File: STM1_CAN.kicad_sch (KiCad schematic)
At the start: 18 parts, among them J6 Conn_01x04, U1 STM32F072C8Tx, U2 TJA1051T-3

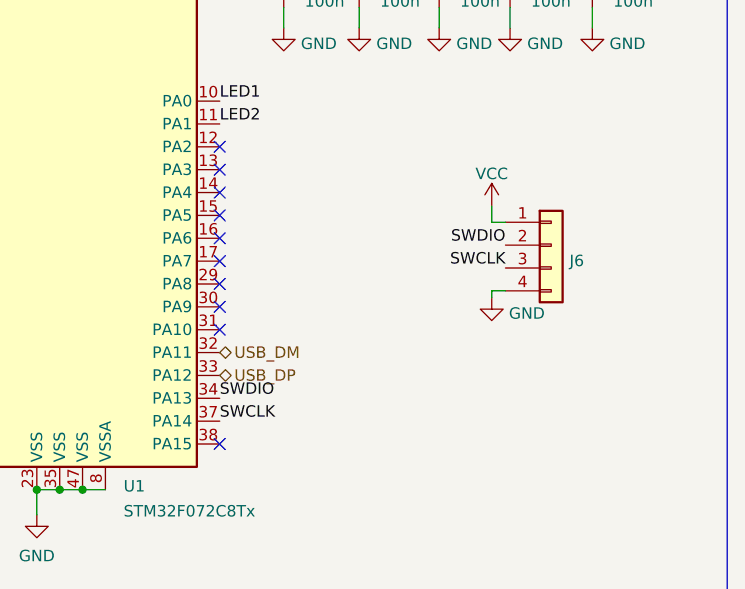
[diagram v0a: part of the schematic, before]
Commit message: New PCB design and single panel to SMT
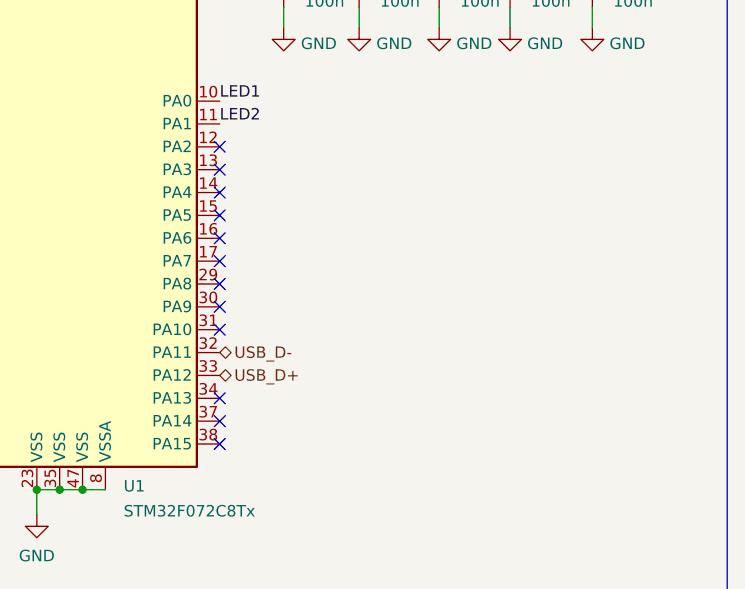
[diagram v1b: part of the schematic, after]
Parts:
- removed J6: Conn_01x04, Connector_JST:JST_GH_BM04B-GHS-TBT_1x04-1MP_P1.25mm_Vertical, symbol Connector_Generic:Conn_01x04
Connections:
- net SWCLK: no longer names the net of U1.37 (PA14)
- net SWDIO: no longer names the net of U1.34 (PA13)
- net USB_DM renamed USB_D-
- net USB_DP renamed USB_D+
- no-connect marks 29 -> 31
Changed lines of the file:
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@@
   (no_connect (at 87.884 84.074))
   (no_connect (at 54.864 99.314))
+  (no_connect (at 87.884 101.854))
+  (no_connect (at 87.884 104.394))
   (no_connect (at 87.884 91.694))
   (no_connect (at 87.884 86.614))
@@
     (stroke (width 0) (type default) (color 0 0 0 0))
   )
-  (wire (pts (xy 118.11 90.678) (xy 118.11 89.916))
-    (stroke (width 0) (type default) (color 0 0 0 0))
-  )
   (wire (pts (xy 112.268 50.8) (xy 112.268 53.34))
     (stroke (width 0) (type default) (color 0 0 0 0))
@@
     (stroke (width 0) (type default) (color 0 0 0 0))
   )
-  (wire (pts (xy 118.11 89.916) (xy 119.634 89.916))
-    (stroke (width 0) (type default) (color 0 0 0 0))
-  )
   (wire (pts (xy 44.196 40.894) (xy 48.006 40.894))
     (stroke (width 0) (type default) (color 0 0 0 0))
@@
     (stroke (width 0) (type default) (color 0 0 0 0))
   )
-  (wire (pts (xy 118.11 82.296) (xy 119.634 82.296))
-    (stroke (width 0) (type default) (color 0 0 0 0))
-  )
   (wire (pts (xy 129.286 58.42) (xy 129.286 60.706))
     (stroke (width 0) (type default) (color 0 0 0 0))
@@
   )
   (wire (pts (xy 125.984 156.972) (xy 128.27 156.972))
-    (stroke (width 0) (type default) (color 0 0 0 0))
-  )
-  (wire (pts (xy 118.11 80.518) (xy 118.11 82.296))
     (stroke (width 0) (type default) (color 0 0 0 0))
   )
@@
     (effects (font (size 1.27 1.27)) (justify left bottom))
   )
-  (label "SWCLK" (at 87.884 104.394 0)
-    (effects (font (size 1.27 1.27)) (justify left bottom))
-  )
-  (label "SWDIO" (at 87.884 101.854 0)
-    (effects (font (size 1.27 1.27)) (justify left bottom))
-  )
   (label "CAN_TX" (at 54.864 91.694 180)
     (effects (font (size 1.27 1.27)) (justify right bottom))
@@
     (effects (font (size 1.27 1.27)) (justify right bottom))
   )
-  (label "SWCLK" (at 119.634 87.376 180)
-    (effects (font (size 1.27 1.27)) (justify right bottom))
-  )
-  (label "SWDIO" (at 119.634 84.836 180)
-    (effects (font (size 1.27 1.27)) (justify right bottom))
-  )
   (label "CAN_RX" (at 100.584 151.892 180)
     (effects (font (size 1.27 1.27)) (justify right bottom))
   )
-  (hierarchical_label "USB_DP" (shape bidirectional) (at 87.884 99.314 0)
+  (hierarchical_label "USB_D+" (shape bidirectional) (at 87.884 99.314 0)
     (effects (font (size 1.27 1.27)) (justify left))
   )
-  (hierarchical_label "USB_DM" (shape bidirectional) (at 87.884 96.774 0)
+  (hierarchical_label "USB_D-" (shape bidirectional) (at 87.884 96.774 0)
     (effects (font (size 1.27 1.27)) (justify left))
   )
@@
     (pin "1")
   )
-  (symbol (lib_id "power:VCC") (at 118.11 80.518 0) (unit 1)
-    (in_bom yes) (on_board yes) (fields_autoplaced)
-    (property "Reference" "#PWR035" (id 0) (at 118.11 84.328 0)
-      (effects (font (size 1.27 1.27)) hide)
-    )
-    (property "Value" "VCC" (id 1) (at 118.11 76.9135 0))
-    (property "Footprint" "" (id 2) (at 118.11 80.518 0)
-      (effects (font (size 1.27 1.27)) hide)
-    )
-    (property "Datasheet" "" (id 3) (at 118.11 80.518 0)
-      (effects (font (size 1.27 1.27)) hide)
-    )
-    (pin "1")
-  )
   (symbol (lib_id "power:VCC") (at 94.996 50.8 0) (unit 1)
     (in_bom yes) (on_board yes) (fields_autoplaced)
@@
     )
     (property "Datasheet" "" (id 3) (at 83.312 166.37 0)
-      (effects (font (size 1.27 1.27)) hide)
-    )
-    (pin "1")
-  )
-  (symbol (lib_id "power:GND") (at 118.11 90.678 0) (unit 1)
-    (in_bom yes) (on_board yes) (fields_autoplaced)
-    (property "Reference" "#PWR036" (id 0) (at 118.11 97.028 0)
-      (effects (font (size 1.27 1.27)) hide)
-    )
-    (property "Value" "GND" (id 1) (at 120.015 92.427 0)
-      (effects (font (size 1.27 1.27)) (justify left))
-    )
-    (property "Footprint" "" (id 2) (at 118.11 90.678 0)
-      (effects (font (size 1.27 1.27)) hide)
-    )
-    (property "Datasheet" "" (id 3) (at 118.11 90.678 0)
       (effects (font (size 1.27 1.27)) hide)
     )
@@
     (pin "2")
   )
-  (symbol (lib_id "Connector_Generic:Conn_01x04") (at 124.714 84.836 0) (unit 1)
-    (in_bom yes) (on_board yes) (fields_autoplaced)
-    (property "Reference" "J6" (id 0) (at 126.746 86.585 0)
-      (effects (font (size 1.27 1.27)) (justify left))
-    )
-    (property "Value" "Conn_01x04" (id 1) (at 124.714 79.8346 0)
-      (effects (font (size 1.27 1.27)) hide)
-    )
-    (property "Footprint" "Connector_JST:JST_GH_BM04B-GHS-TBT_1x04-1MP_P1.25mm_Vertical" (id 2) (at 124.714 84.836 0)
-      (effects (font (size 1.27 1.27)) hide)
-    )
-    (property "Datasheet" "~" (id 3) (at 124.714 84.836 0)
-      (effects (font (size 1.27 1.27)) hide)
-    )
-    (pin "1")
-    (pin "2")
-    (pin "3")
-    (pin "4")
-  )
   (symbol (lib_id "power:GND") (at 129.286 60.706 0) (unit 1)
